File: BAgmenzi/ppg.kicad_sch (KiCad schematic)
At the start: 10 parts, among them U9 MAXM86161EFD_T

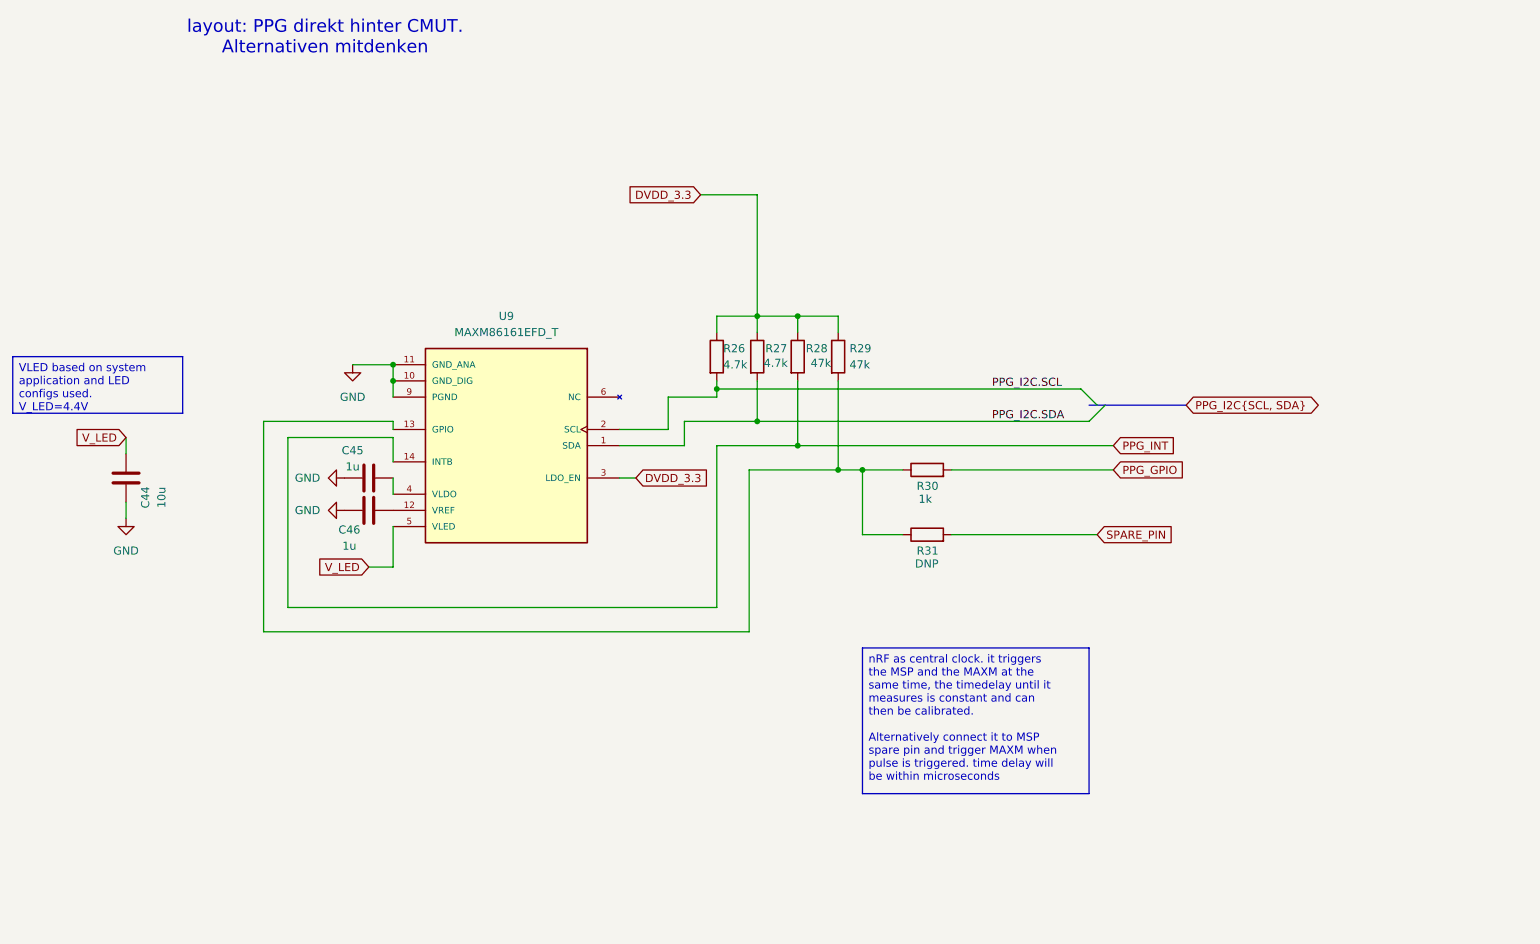
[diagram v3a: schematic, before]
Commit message: part numbers added
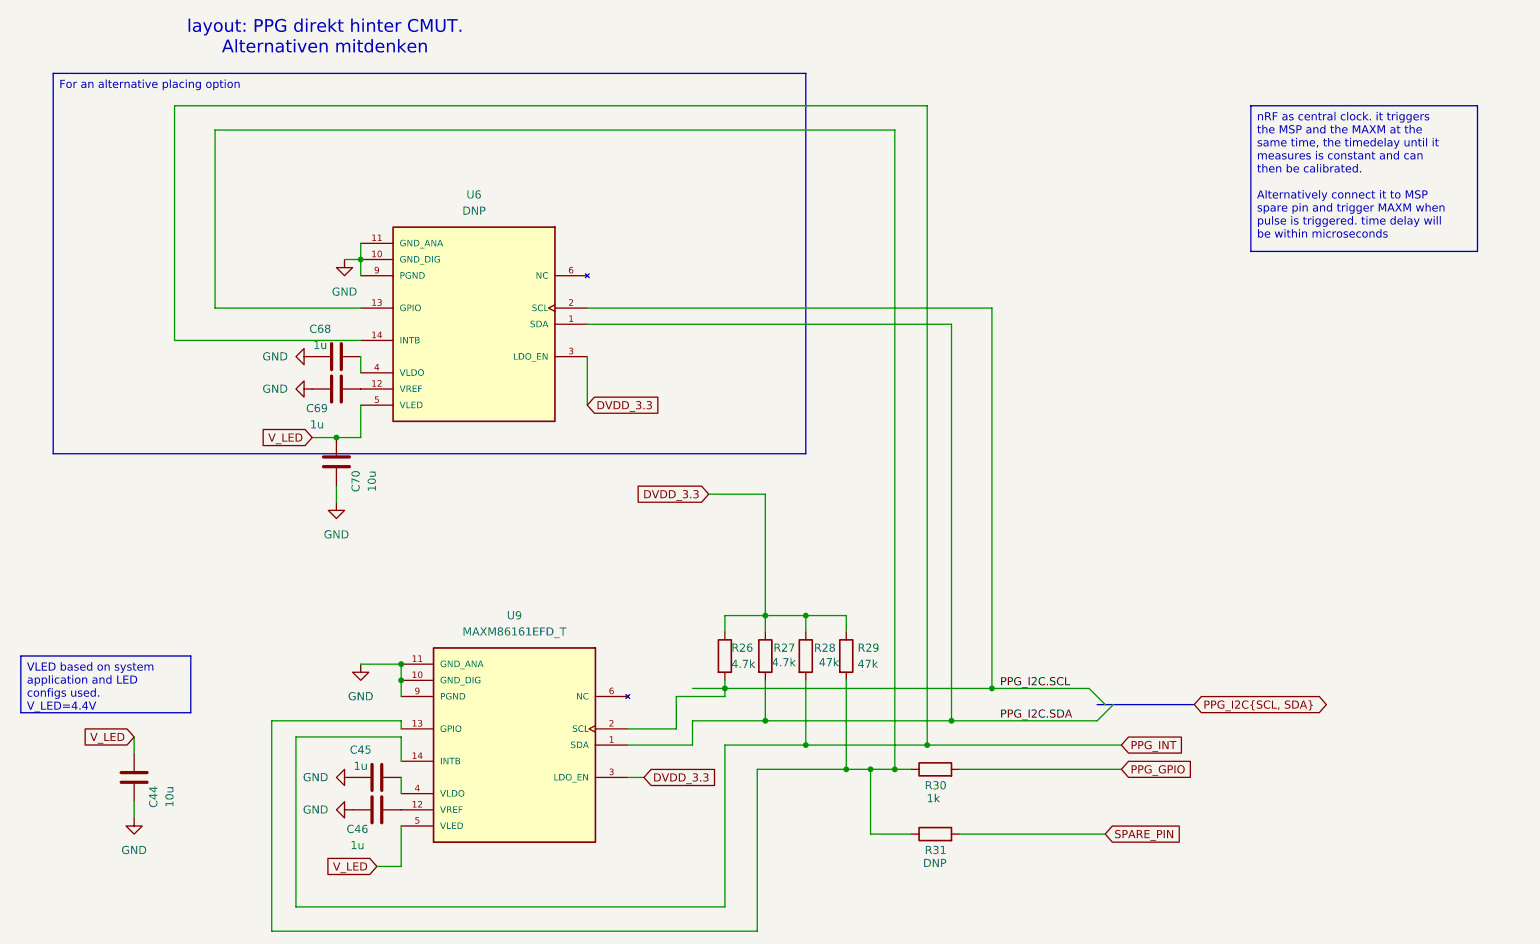
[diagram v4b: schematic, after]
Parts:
- added C68, C69: 1u, Capacitor_SMD:C_0402_1005Metric, symbol Device:C
- added C70: 10u, Capacitor_SMD:C_0402_1005Metric, symbol Device:C
- added U6: DNP, MAXM86161EFD_T:PSON60P430X290X150-14N, symbol MAXM86161EFD_T:MAXM86161EFD_T
- C44: LCSC Part # (none) -> C15525
- C45, C46: LCSC Part # (none) -> C20441333
- R26, R27: LCSC Part # (none) -> C423829
- R28, R29: LCSC Part # (none) -> C880417
- R30: LCSC Part # (none) -> C606165
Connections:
- net DVDD_3.3: now also U6.3 (LDO_EN)
- net GND: now also C68.1, C69.1, C70.1, U6.10 (GND_DIG), U6.11 (GND_ANA), U6.9 (PGND)
- net PPG_I2C.SCL: now also U6.2 (SCL)
- net PPG_I2C.SDA: now also U6.1 (SDA)
- net PPG_INT: now also U6.14 (INTB)
- net V_LED: now also C70.2, U6.5 (VLED)
- net at R29.2, R30.1, R31.1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: now also U6.13 (GPIO)
- new net: C68.2, U6.4 (VLDO)
- new net: C69.2, U6.12 (VREF)
- new net: U6.6 (NC), U6.7 (NC), U6.8 (NC)
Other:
- moved on the sheet: C44, C45, C46, R26, R27, R28, R29, R30, R31, U9

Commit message: LCSC parts complete, changed L5andL6 footprint
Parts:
- C45, C46, C68, C69: LCSC Part # C20441333 -> C14445
- R26, R27: LCSC Part # C423829 -> C25900
- R28, R29: LCSC Part # C880417 -> C482184
- R30: LCSC Part # C606165 -> C11702
- U9: LCSC Part # (none) -> C3178309
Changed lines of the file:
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@@
 			)
 		)
-		(property "LCSC Part #" "C20441333"
+		(property "LCSC Part #" "C14445 "
 			(at 86.36 142.24 90)
 			(effects
@@
 			)
 		)
-		(property "LCSC Part #" "C20441333"
+		(property "LCSC Part #" "C14445 "
 			(at 86.36 147.32 90)
 			(effects
@@
 			)
 		)
-		(property "LCSC Part #" "C423829"
+		(property "LCSC Part #" "C25900 "
 			(at 140.97 123.19 0)
 			(effects
@@
 			)
 		)
-		(property "LCSC Part #" "C880417"
+		(property "LCSC Part #" "C482184 "
 			(at 160.02 123.19 0)
 			(effects
@@
 			)
 		)
-		(property "LCSC Part #" "C20441333"
+		(property "LCSC Part #" "C14445 "
 			(at 80.01 76.2 90)
 			(effects
@@
 			)
 		)
+		(property "LCSC Part #" "C3178309 "
+			(at 107.95 137.16 0)
+			(effects
+				(font
+					(size 1.27 1.27)
+				)
+				(hide yes)
+			)
+		)
 		(pin "4"
 		)
@@
 			)
 		)
-		(property "LCSC Part #" "C880417"
+		(property "LCSC Part #" "C482184 "
 			(at 153.67 123.19 0)
 			(effects
@@
 			)
 		)
-		(property "LCSC Part #" "C423829"
+		(property "LCSC Part #" "C25900 "
 			(at 147.32 123.19 0)
 			(effects
@@
 			)
 		)
-		(property "LCSC Part #" "C606165"
+		(property "LCSC Part #" "C11702 "
 			(at 173.99 140.97 90)
 			(effects
@@
 			)
 		)
-		(property "LCSC Part #" "C20441333"
+		(property "LCSC Part #" "C14445 "
 			(at 80.01 81.28 90)
 			(effects

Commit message: corrected LCSC numbers, other changes, Testpoints
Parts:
- C44, C70: LCSC Part # C15525 -> C15525
- C45, C46, C68, C69: LCSC Part # C14445 -> C14445
- R26, R27: LCSC Part # C25900 -> C25900
- R28, R29: LCSC Part # C482184 -> C482184
- R30: LCSC Part # C11702 -> C11702
- R31: now not fitted
- U6: now not fitted; now left out of the parts list
- U9: LCSC Part # C3178309 -> C3178309
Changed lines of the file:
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@@
 			)
 		)
-		(property "LCSC Part #" "C14445 "
+		(property "LCSC Part #" "C14445"
 			(at 86.36 142.24 90)
 			(effects
@@
 			)
 		)
-		(property "LCSC Part #" "C14445 "
+		(property "LCSC Part #" "C14445"
 			(at 86.36 147.32 90)
 			(effects
@@
 			)
 		)
-		(property "LCSC Part #" "C25900 "
+		(property "LCSC Part #" "C25900"
 			(at 140.97 123.19 0)
 			(effects
@@
 			)
 		)
-		(property "LCSC Part #" "C482184 "
+		(property "LCSC Part #" "C482184"
 			(at 160.02 123.19 0)
 			(effects
@@
 			)
 		)
-		(property "LCSC Part #" "C14445 "
+		(property "LCSC Part #" "C14445"
 			(at 80.01 76.2 90)
 			(effects
@@
 			)
 		)
-		(property "LCSC Part #" "C3178309 "
+		(property "LCSC Part #" "C3178309"
 			(at 107.95 137.16 0)
 			(effects
@@
 		(unit 1)
 		(exclude_from_sim no)
-		(in_bom yes)
-		(on_board yes)
-		(dnp no)
+		(in_bom no)
+		(on_board yes)
+		(dnp yes)
 		(fields_autoplaced yes)
 		(property "Reference" "U6"
@@
 			)
 		)
-		(property "LCSC Part #" "C482184 "
+		(property "LCSC Part #" "C482184"
 			(at 153.67 123.19 0)
 			(effects
@@
 		(in_bom yes)
 		(on_board yes)
-		(dnp no)
+		(dnp yes)
 		(property "Reference" "R31"
 			(at 175.768 153.67 90)
@@
 			)
 		)
-		(property "LCSC Part #" "C25900 "
+		(property "LCSC Part #" "C25900"
 			(at 147.32 123.19 0)
 			(effects
@@
 			)
 		)
-		(property "LCSC Part #" "C11702 "
+		(property "LCSC Part #" "C11702"
 			(at 173.99 140.97 90)
 			(effects
@@
 			)
 		)
-		(property "LCSC Part #" "C15525 "
+		(property "LCSC Part #" "C15525"
 			(at 48.26 142.24 90)
 			(effects
@@
 			)
 		)
-		(property "LCSC Part #" "C15525 "
+		(property "LCSC Part #" "C15525"
 			(at 80.01 92.71 90)
 			(effects
@@
 			)
 		)
-		(property "LCSC Part #" "C14445 "
+		(property "LCSC Part #" "C14445"
 			(at 80.01 81.28 90)
 			(effects
